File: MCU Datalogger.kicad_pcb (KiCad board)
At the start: 2 copper layers, 29 parts, among them J1 Conn_01x09_Male, J2 Conn_01x04_Male, J3 Conn_02x03_Odd_Even, J4 Conn_01x04_Male, U1 24LC1025, U2 DS1337S+, U3 24LC1025, U4 ATMEGA328P-AU, Y1 32.768 KHz, Y2 16MHz

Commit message: Initial positioning of the footprints
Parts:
- moved H3 95.0 mm to (80.5, 78.3)
- moved J1 92.2 mm to (85.0, 104.3), turned to 90 degrees
- moved BT1 89.7 mm to (80.0, 82.6)
- moved C1 88.4 mm to (95.4, 77.8)
- moved C5 87.8 mm to (104.3, 77.6)
- moved C3 85.6 mm to (99.9, 77.5)
- moved R1 84.0 mm to (84.9, 100.4)
- moved J3 81.9 mm to (124.0, 82.9)
- moved D1 81.0 mm to (119.4, 78.1)
- moved R2 80.4 mm to (89.0, 100.4), turned to 180 degrees
- moved U1 80.1 mm to (88.1, 80.1)
- moved H4 79.6 mm to (80.5, 103.8)
- moved Y1 78.2 mm to (80.6, 94.7), turned to -90 degrees
- moved R5 76.6 mm to (119.3, 81.6)
- moved R7 75.8 mm to (115.4, 81.6)
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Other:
- board outline added: 50 x 30 mm

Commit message: Routing in progress
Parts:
- moved U3 7.50 mm to (88.4, 79.3)
- moved U1 5.52 mm to (88.3, 85.6)
- moved Y2 2.42 mm to (97.5, 99.0), turned to 180 degrees
- moved BT1 1.37 mm to (80.0, 83.9)
- moved U2 1.21 mm to (88.1, 92.9)
- moved C3 0.77 mm to (99.2, 77.4)
- moved C1 0.41 mm to (95.2, 77.4)
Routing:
- net GND: track 0.00 -> 37.6 mm, vias 0 -> 2
- net /Vcc: track 0.00 -> 21.6 mm
- net Net-(R1-Pad2): track 0.00 -> 12.3 mm
- net Net-(C2-Pad2): track 0.00 -> 11.4 mm
- net Net-(C3-Pad2): track 0.00 -> 9.52 mm
- net Net-(R2-Pad2): track 0.00 -> 9.38 mm
- net Net-(U2-Pad2): track 0.00 -> 7.47 mm
- net Net-(U2-Pad1): track 0.00 -> 5.52 mm
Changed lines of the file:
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@@
   )
   (footprint "Package_SO:SOIC-8_5.23x5.23mm_P1.27mm" (layer "F.Cu")
-    (at 88.0872 80.0862)
+    (at 88.2904 85.598)
     (descr "SOIC, 8 Pin (http://www.winbond.com/resource-files/w25q32jv%20revg%2003272018%20plus.pdf#page=68), generated with kicad-footprint-generator ipc_gullwing_generator.py")
     (tags "SOIC SO")
@@
   )
   (footprint "Package_SO:SOIC-8_5.23x5.23mm_P1.27mm" (layer "F.Cu")
-    (at 88.0872 86.8172)
+    (at 88.392 79.3242)
     (descr "SOIC, 8 Pin (http://www.winbond.com/resource-files/w25q32jv%20revg%2003272018%20plus.pdf#page=68), generated with kicad-footprint-generator ipc_gullwing_generator.py")
     (tags "SOIC SO")
@@
   )
   (footprint "Capacitor_SMD:C_0805_2012Metric" (layer "F.Cu")
-    (at 95.4278 77.8002)
+    (at 95.2246 77.4446)
     (descr "Capacitor SMD 0805 (2012 Metric), square (rectangular) end terminal, IPC_7351 nominal, (Body size source: IPC-SM-782 page 76, https://www.pcb-3d.com/wordpress/wp-content/uploads/ipc-sm-782a_amendment_1_and_2.pdf, https://docs.google.com/spreadsheets/d/1BsfQQcO9C6DZCsRaXUlFlo91Tg2WpOkGARC1WS5S8t0/edit?usp=sharing), generated with kicad-footprint-generator")
     (tags "capacitor")
@@
   )
   (footprint "Crystal:Crystal_SMD_5032-2Pin_5.0x3.2mm_HandSoldering" (layer "F.Cu")
-    (at 99.8474 99.3902)
+    (at 97.4598 99.0092 180)
     (descr "SMD Crystal SERIES SMD2520/2 http://www.icbase.com/File/PDF/HKC/HKC00061008.pdf, hand-soldering, 5.0x3.2mm^2 package")
     (tags "SMD SMT crystal hand-soldering")
@@
     (fp_line (start 2.3 1.6) (end -2.3 1.6) (layer "F.Fab") (width 0.1))
     (fp_line (start -2.5 -1.4) (end -2.3 -1.6) (layer "F.Fab") (width 0.1))
-    (pad "1" smd rect (at -2.6 0) (size 3.5 2.4) (layers "F.Cu" "F.Paste" "F.Mask")
+    (pad "1" smd rect (at -2.6 0 180) (size 3.5 2.4) (layers "F.Cu" "F.Paste" "F.Mask")
       (net 5 "Net-(C3-Pad2)") (pinfunction "1") (pintype "passive"))
-    (pad "2" smd rect (at 2.6 0) (size 3.5 2.4) (layers "F.Cu" "F.Paste" "F.Mask")
+    (pad "2" smd rect (at 2.6 0 180) (size 3.5 2.4) (layers "F.Cu" "F.Paste" "F.Mask")
       (net 4 "Net-(C2-Pad2)") (pinfunction "2") (pintype "passive"))
     (model "${KICAD6_3DMODEL_DIR}/Crystal.3dshapes/Crystal_SMD_5032-2Pin_5.0x3.2mm_HandSoldering.wrl"
@@
   )
   (footprint "Connector_PinHeader_2.54mm:PinHeader_1x02_P2.54mm_Vertical" (layer "F.Cu")
-    (at 80.01 82.5754)
+    (at 80.01 83.942)
     (descr "Through hole straight pin header, 1x02, 2.54mm pitch, single row")
     (tags "Through hole pin header THT 1x02 2.54mm single row")
@@
   )
   (footprint "Footprints:SOIC127P600X175-8N" (layer "F.Cu")
-    (at 87.9348 94.1324)
+    (at 88.138 92.9386)
     (property "Sheetfile" "MCU Datalogger.kicad_sch")
     (property "Sheetname" "")
@@
       (effects (font (size 1 1) (thickness 0.15)))
     )
-    (fp_text value "DS1337S+" (at 7.46 3.332) (layer "F.Fab")
+    (fp_text value "DS1337S+" (at 0.0276 3.683) (layer "F.Fab")
       (effects (font (size 1 1) (thickness 0.15)))
     )
@@
   )
   (footprint "Capacitor_SMD:C_0805_2012Metric" (layer "F.Cu")
-    (at 99.949 77.47)
+    (at 99.187 77.3938)
     (descr "Capacitor SMD 0805 (2012 Metric), square (rectangular) end terminal, IPC_7351 nominal, (Body size source: IPC-SM-782 page 76, https://www.pcb-3d.com/wordpress/wp-content/uploads/ipc-sm-782a_amendment_1_and_2.pdf, https://docs.google.com/spreadsheets/d/1BsfQQcO9C6DZCsRaXUlFlo91Tg2WpOkGARC1WS5S8t0/edit?usp=sharing), generated with kicad-footprint-generator")
     (tags "capacitor")
@@
   )
   (gr_rect (start 78.2574 76.073) (end 128.27 106.0958) (layer "Edge.Cuts") (width 0.1) (fill none))
+  (segment (start 80.01 86.482) (end 81.031 87.503) (width 0.35) (layer "F.Cu") (net 2))
+  (segment (start 98.1862 77.4446) (end 98.237 77.3938) (width 0.35) (layer "F.Cu") (net 2))
+  (segment (start 78.735489 85.207489) (end 78.735489 82.667489) (width 0.35) (layer "F.Cu") (net 2))
+  (segment (start 85.663 94.8436) (end 87.249 94.8436) (width 0.35) (layer "F.Cu") (net 2))
+  (segment (start 87.5792 78.6892) (end 91.992 78.6892) (width 0.35) (layer "F.Cu") (net 2))
+  (segment (start 84.792 78.6892) (end 87.5792 78.6892) (width 0.35) (layer "F.Cu") (net 2))
+  (segment (start 96.1746 77.4446) (end 98.1862 77.4446) (width 0.35) (layer "F.Cu") (net 2))
+  (segment (start 91.8904 84.963) (end 90.5764 84.963) (width 0.35) (layer "F.Cu") (net 2))
+  (segment (start 81.031 87.503) (end 84.6904 87.503) (width 0.35) (layer "F.Cu") (net 2))
+  (segment (start 87.5792 78.784493) (end 87.5792 78.6892) (width 0.35) (layer "F.Cu") (net 2))
+  (segment (start 94.93 78.6892) (end 96.1746 77.4446) (width 0.35) (layer "F.Cu") (net 2))
+  (segment (start 84.792 81.2292) (end 85.134493 81.2292) (width 0.35) (layer "F.Cu") (net 2))
+  (segment (start 80.01 86.482) (end 78.735489 85.207489) (width 0.35) (layer "F.Cu") (net 2))
+  (segment (start 87.249 94.8436) (end 87.4776 94.615) (width 0.35) (layer "F.Cu") (net 2))
+  (segment (start 80.173778 81.2292) (end 84.792 81.2292) (width 0.35) (layer "F.Cu") (net 2))
+  (segment (start 78.735489 82.667489) (end 80.173778 81.2292) (width 0.35) (layer "F.Cu") (net 2))
+  (segment (start 90.5764 84.963) (end 90.297 84.6836) (width 0.35) (layer "F.Cu") (net 2))
+  (segment (start 91.992 78.6892) (end 94.93 78.6892) (width 0.35) (layer "F.Cu") (net 2))
+  (segment (start 85.134493 81.2292) (end 87.5792 78.784493) (width 0.35) (layer "F.Cu") (net 2))
+  (via (at 90.297 84.6836) (size 0.9) (drill 0.4) (layers "F.Cu" "B.Cu") (net 2))
+  (via (at 87.4776 94.615) (size 0.9) (drill 0.4) (layers "F.Cu" "B.Cu") (net 2))
+  (segment (start 84.6904 84.963) (end 84.6904 86.233) (width 0.35) (layer "F.Cu") (net 3))
+  (segment (start 83.9489 100.3808) (end 85.07342 99.25628) (width 0.35) (layer "F.Cu") (net 3))
+  (segment (start 88.71338 101.50532) (end 89.8633 100.3554) (width 0.35) (layer "F.Cu") (net 3))
+  (segment (start 91.992 77.4192) (end 94.2492 77.4192) (width 0.35) (layer "F.Cu") (net 3))
+  (segment (start 85.8012 86.233) (end 88.3412 83.693) (width 0.35) (layer "F.Cu") (net 3))
+  (segment (start 94.2492 77.4192) (end 94.2746 77.4446) (width 0.35) (layer "F.Cu") (net 3))
+  (segment (start 88.73878 101.47992) (end 88.78475 101.43395) (width 0.35) (layer "F.Cu") (net 3))
+  (segment (start 84.6904 83.693) (end 84.6904 84.963) (width 0.35) (layer "F.Cu") (net 3))
+  (segment (start 87.10128 100.02988) (end 87.10128 101.084795) (width 0.35) (layer "F.Cu") (net 3))
+  (segment (start 84.6904 86.233) (end 85.8012 86.233) (width 0.35) (layer "F.Cu") (net 3))
+  (segment (start 86.32768 99.25628) (end 87.10128 100.02988) (width 0.35) (layer "F.Cu") (net 3))
+  (segment (start 87.496405 101.47992) (end 88.73878 101.47992) (width 0.35) (layer "F.Cu") (net 3))
+  (segment (start 87.10128 101.084795) (end 87.496405 101.47992) (width 0.35) (layer "F.Cu") (net 3))
+  (segment (start 85.07342 99.25628) (end 86.32768 99.25628) (width 0.35) (layer "F.Cu") (net 3))
+  (segment (start 88.3412 83.693) (end 91.8904 83.693) (width 0.35) (layer "F.Cu") (net 3))
+  (segment (start 94.8598 99.0092) (end 96.4946 97.3744) (width 0.25) (layer "F.Cu") (net 4))
+  (segment (start 96.4946 97.3744) (end 96.4946 90.272578) (width 0.25) (layer "F.Cu") (net 4))
+  (segment (start 97.264178 89.503) (end 98.1382 89.503) (width 0.25) (layer "F.Cu") (net 4))
+  (segment (start 96.4946 90.272578) (end 97.264178 89.503) (width 0.25) (layer "F.Cu") (net 4))
+  (segment (start 98.1202 96.2914) (end 98.1382 96.2734) (width 0.25) (layer "F.Cu") (net 5))
+  (segment (start 100.0598 99.0092) (end 98.1202 97.0696) (width 0.25) (layer "F.Cu") (net 5))
+  (segment (start 98.1382 96.2734) (end 98.1382 90.303) (width 0.25) (layer "F.Cu") (net 5))
+  (segment (start 98.1202 97.0696) (end 98.1202 96.2914) (width 0.25) (layer "F.Cu") (net 5))
+  (segment (start 83.427716 101.45532) (end 83.058 101.085604) (width 0.25) (layer "F.Cu") (net 23))
+  (segment (start 85.7739 100.3808) (end 84.69938 101.45532) (width 0.25) (layer "F.Cu") (net 23))
+  (segment (start 83.058 95.5802) (end 85.0646 93.5736) (width 0.25) (layer "F.Cu") (net 23))
+  (segment (start 83.058 101.085604) (end 83.058 95.5802) (width 0.25) (layer "F.Cu") (net 23))
+  (segment (start 85.0646 93.5736) (end 85.663 93.5736) (width 0.25) (layer "F.Cu") (net 23))
+  (segment (start 84.69938 101.45532) (end 83.427716 101.45532) (width 0.25) (layer "F.Cu") (net 23))
+  (segment (start 90.168253 92.3036) (end 90.613 92.3036) (width 0.25) (layer "F.Cu") (net 24))
+  (segment (start 88.0383 100.3554) (end 89.2048 99.1889) (width 0.25) (layer "F.Cu") (net 24))
+  (segment (start 89.2048 99.1889) (end 89.2048 93.267053) (width 0.25) (layer "F.Cu") (net 24))
+  (segment (start 89.2048 93.267053) (end 90.168253 92.3036) (width 0.25) (layer "F.Cu") (net 24))
+  (segment (start 81.601 91.0336) (end 80.5688 92.0658) (width 0.25) (layer "F.Cu") (net 25))
+  (segment (start 85.663 91.0336) (end 81.601 91.0336) (width 0.25) (layer "F.Cu") (net 25))
+  (segment (start 80.5688 97.2658) (end 80.5688 96.7158) (width 0.25) (layer "F.Cu") (net 26))
+  (segment (start 80.5688 96.7158) (end 84.981 92.3036) (width 0.25) (layer "F.Cu") (net 26))
+  (segment (start 84.981 92.3036) (end 85.663 92.3036) (width 0.25) (layer "F.Cu") (net 26))
 )

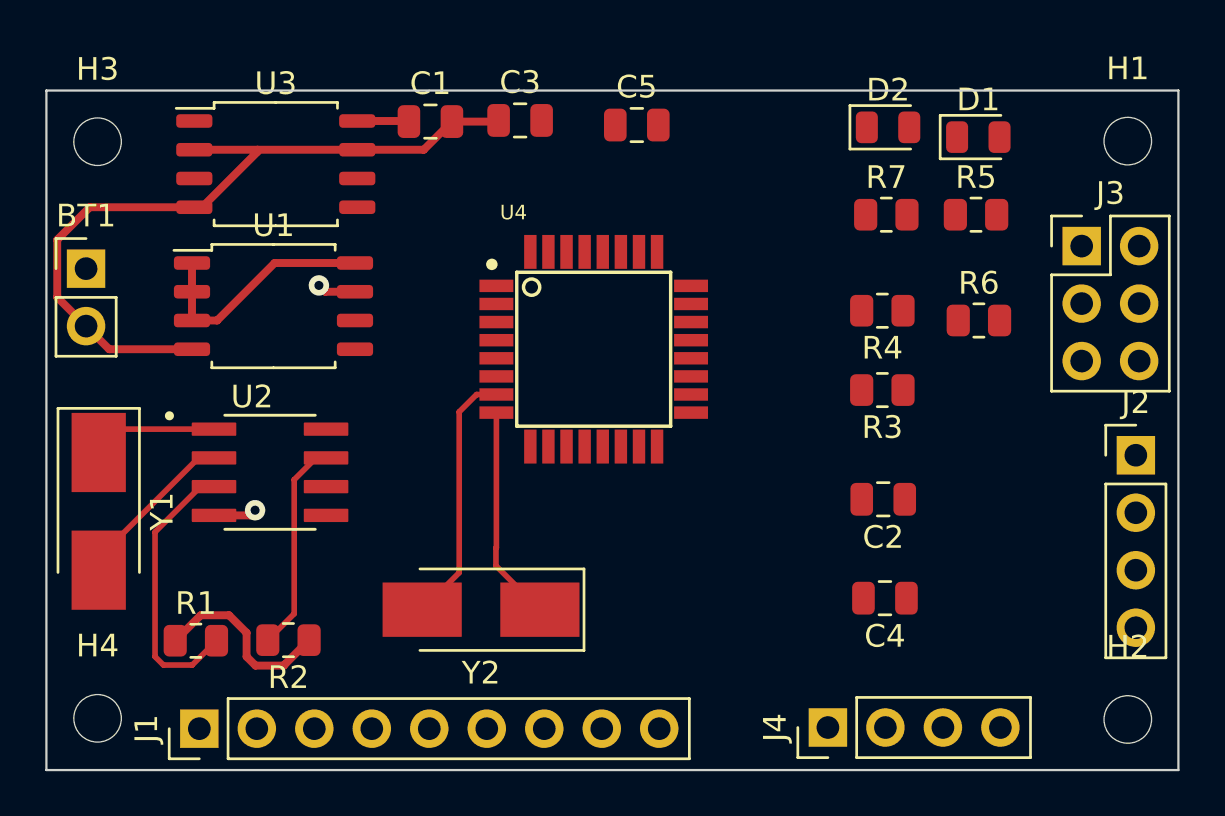
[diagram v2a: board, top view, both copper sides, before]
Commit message: added some additional routing
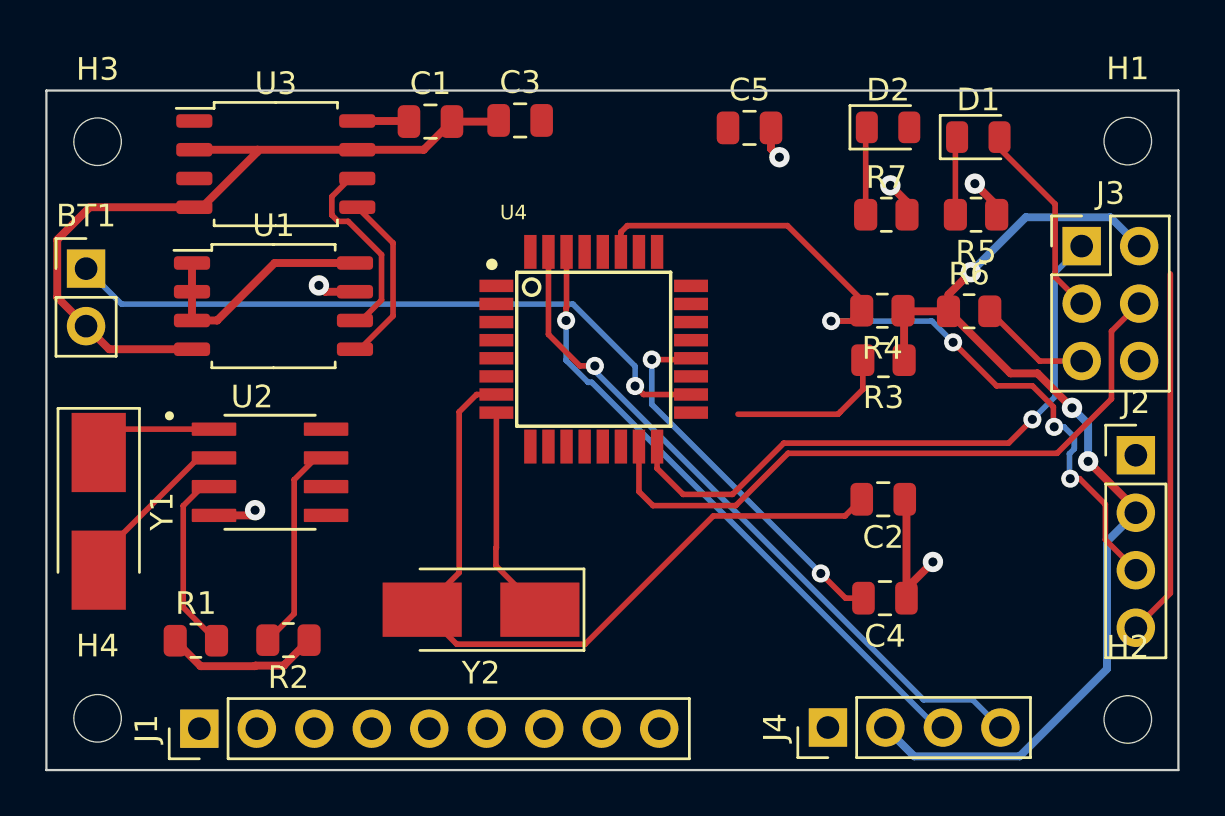
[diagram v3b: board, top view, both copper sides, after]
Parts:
- moved C5 4.98 mm to (109.3, 77.7)
- moved R3 1.32 mm to (115.2, 88.0)
- moved R6 0.59 mm to (119.0, 85.8)
- turned R5 to 180 degrees
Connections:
- J3 pad 1: /MOSI -> /MISO
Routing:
- net /Vcc: track 21.6 -> 67.7 mm, vias 0 -> 3
- net /SDA: track 0.00 -> 43.5 mm, vias 0 -> 4
- net /SCL: track 0.00 -> 32.3 mm
- net /TX: track 0.00 -> 30.9 mm, vias 0 -> 1
- net /MOSI: track 0.00 -> 29.8 mm
- net Net-(BT1-Pad1): track 0.00 -> 29.5 mm, vias 0 -> 1
- net /RX: track 0.00 -> 28.2 mm, vias 0 -> 1
- net /MISO: track 0.00 -> 28.0 mm, vias 0 -> 1
- net Net-(C2-Pad2): track 11.4 -> 34.1 mm
- net Net-(C4-Pad2): track 0.00 -> 16.6 mm, vias 0 -> 2
- net GND: track 37.6 -> 49.1 mm, vias 2 -> 6
- net /SCK: track 0.00 -> 8.86 mm
- net /RESET: track 0.00 -> 4.97 mm
- net Net-(D2-Pad1): track 0.00 -> 3.88 mm
- net Net-(D1-Pad1): track 0.00 -> 3.46 mm
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
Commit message: more routing
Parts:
- moved C3 2.57 mm to (101.8, 77.4)
- moved C1 2.49 mm to (97.7, 77.4)
- moved J2 0.21 mm to (126.4, 92.0)
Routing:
- net /SCL: track 32.3 -> 73.8 mm, vias 0 -> 6
- net /D2: track 0.00 -> 34.4 mm, vias 0 -> 2
- net Net-(BT1-Pad1): track 29.5 -> 61.7 mm, vias 1 -> 3
- net /Vcc: track 67.7 -> 93.1 mm
- net /D3: track 0.00 -> 24.5 mm
- net /D4: track 0.00 -> 22.7 mm
- net /RESET: track 4.97 -> 27.5 mm, vias 0 -> 4
- net /D5: track 0.00 -> 21.3 mm
- net /SCK: track 8.86 -> 29.8 mm, vias 0 -> 2
- net /D6: track 0.00 -> 20.0 mm
- net /SDA: track 43.5 -> 62.5 mm
- net /D7: track 0.00 -> 18.0 mm
- net /D8: track 0.00 -> 15.6 mm
- net Net-(C3-Pad2): track 9.52 -> 25.0 mm, vias 0 -> 2
- net Net-(R1-Pad2): track 8.88 -> 12.8 mm
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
